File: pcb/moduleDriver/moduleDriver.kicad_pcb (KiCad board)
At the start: 2 copper layers, 51.4 x 80 mm, 43 parts, among them J1 UART_RL, J10 Sensor, J11 Power, J12 Power, J13 Neopixel, J2 UART_LR, J3 MOTOR, J4 MOTOR, J5 MOTOR, J6 MOTOR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

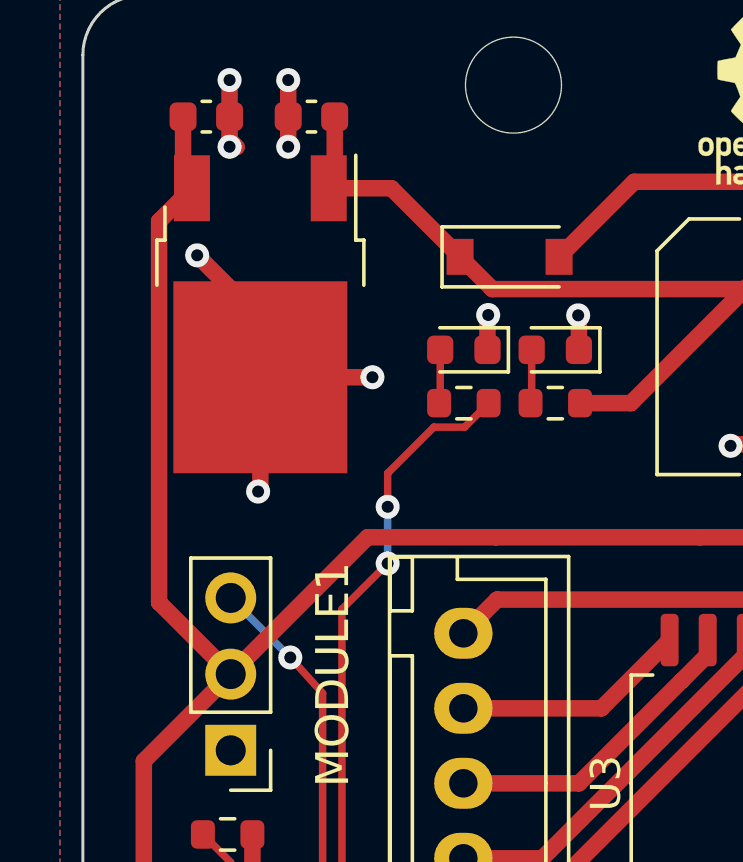
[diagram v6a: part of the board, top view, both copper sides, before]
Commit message: Add more vias for thermal release
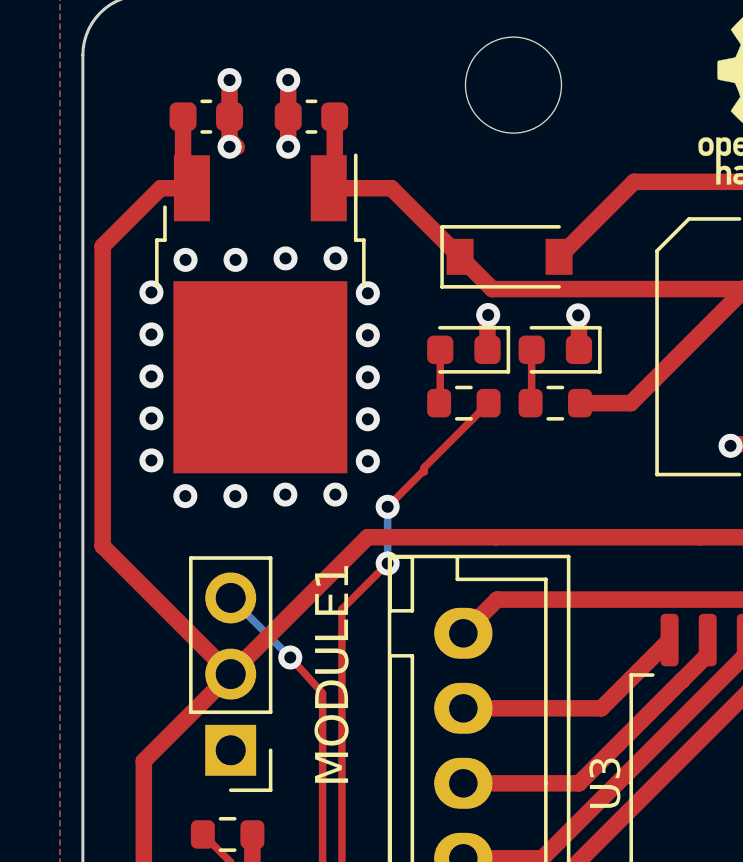
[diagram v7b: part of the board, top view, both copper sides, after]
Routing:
- net GND: track 67.2 -> 56.6 mm, vias 34 -> 49
- net +5V: track 174.4 -> 176.6 mm
- net /LED: track 48.9 -> 48.3 mm
